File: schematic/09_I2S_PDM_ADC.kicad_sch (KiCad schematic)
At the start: 3 parts, among them J16 I2S, J17 PDM, J18 ADC_AIN0-7

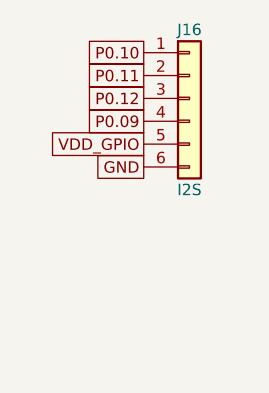
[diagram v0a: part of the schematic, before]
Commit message: Pin remap + PCB sync (pass30cb): UART0 2-wire (RX P0.04, J9.2/3 NC), J16 DNF, U2 TLV73333 on PCB; ERC 0 errors; unconnected 43→38 (26 non-GND + 12 GND); short/clr/cross/hole 0
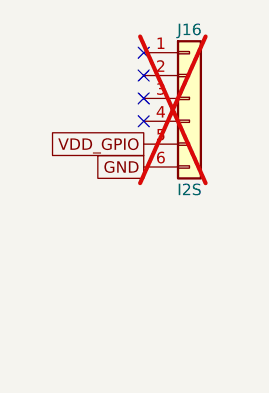
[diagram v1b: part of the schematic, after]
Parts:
- J16: now not fitted; now left out of the parts list
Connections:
- net P0.09: no longer names the net of J16.4 (Pin_4)
- net P0.10: no longer names the net of J16.1 (Pin_1)
- net P0.11: no longer names the net of J16.2 (Pin_2)
- net P0.12: no longer names the net of J16.3 (Pin_3)
- no-connect marks 0 -> 4
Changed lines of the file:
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@@
 		(unit 1)
 		(exclude_from_sim no)
-		(in_bom yes)
+		(in_bom no)
 		(on_board yes)
-		(dnp no)
+		(dnp yes)
 		(property "Reference" "J16"
 			(at 63.5 30.48 0)
@@
 		)
 	)
-	(global_label "P0.10"
-		(at 58.42 33.02 180)
-		(effects
-			(font
-				(size 1.27 1.27)
-			)
-			(justify right)
-		)
-	)
-	(global_label "P0.11"
-		(at 58.42 35.56 180)
-		(effects
-			(font
-				(size 1.27 1.27)
-			)
-			(justify right)
-		)
-	)
-	(global_label "P0.12"
-		(at 58.42 38.1 180)
-		(effects
-			(font
-				(size 1.27 1.27)
-			)
-			(justify right)
-		)
-	)
-	(global_label "P0.09"
-		(at 58.42 40.64 180)
-		(effects
-			(font
-				(size 1.27 1.27)
-			)
-			(justify right)
-		)
-	)
 	(global_label "VDD_GPIO"
 		(at 58.42 43.18 180)
@@
 		)
 	)
+	(no_connect
+		(at 58.42 33.02)
+	)
+	(no_connect
+		(at 58.42 35.56)
+	)
+	(no_connect
+		(at 58.42 38.1)
+	)
+	(no_connect
+		(at 58.42 40.64)
+	)
 	(sheet_instances
